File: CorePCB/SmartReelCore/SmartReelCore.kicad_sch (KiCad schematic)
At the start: 5 parts, among them J1 Screw_Terminal_01x02, J2 Screw_Terminal_01x03, J3 Screw_Terminal_01x04

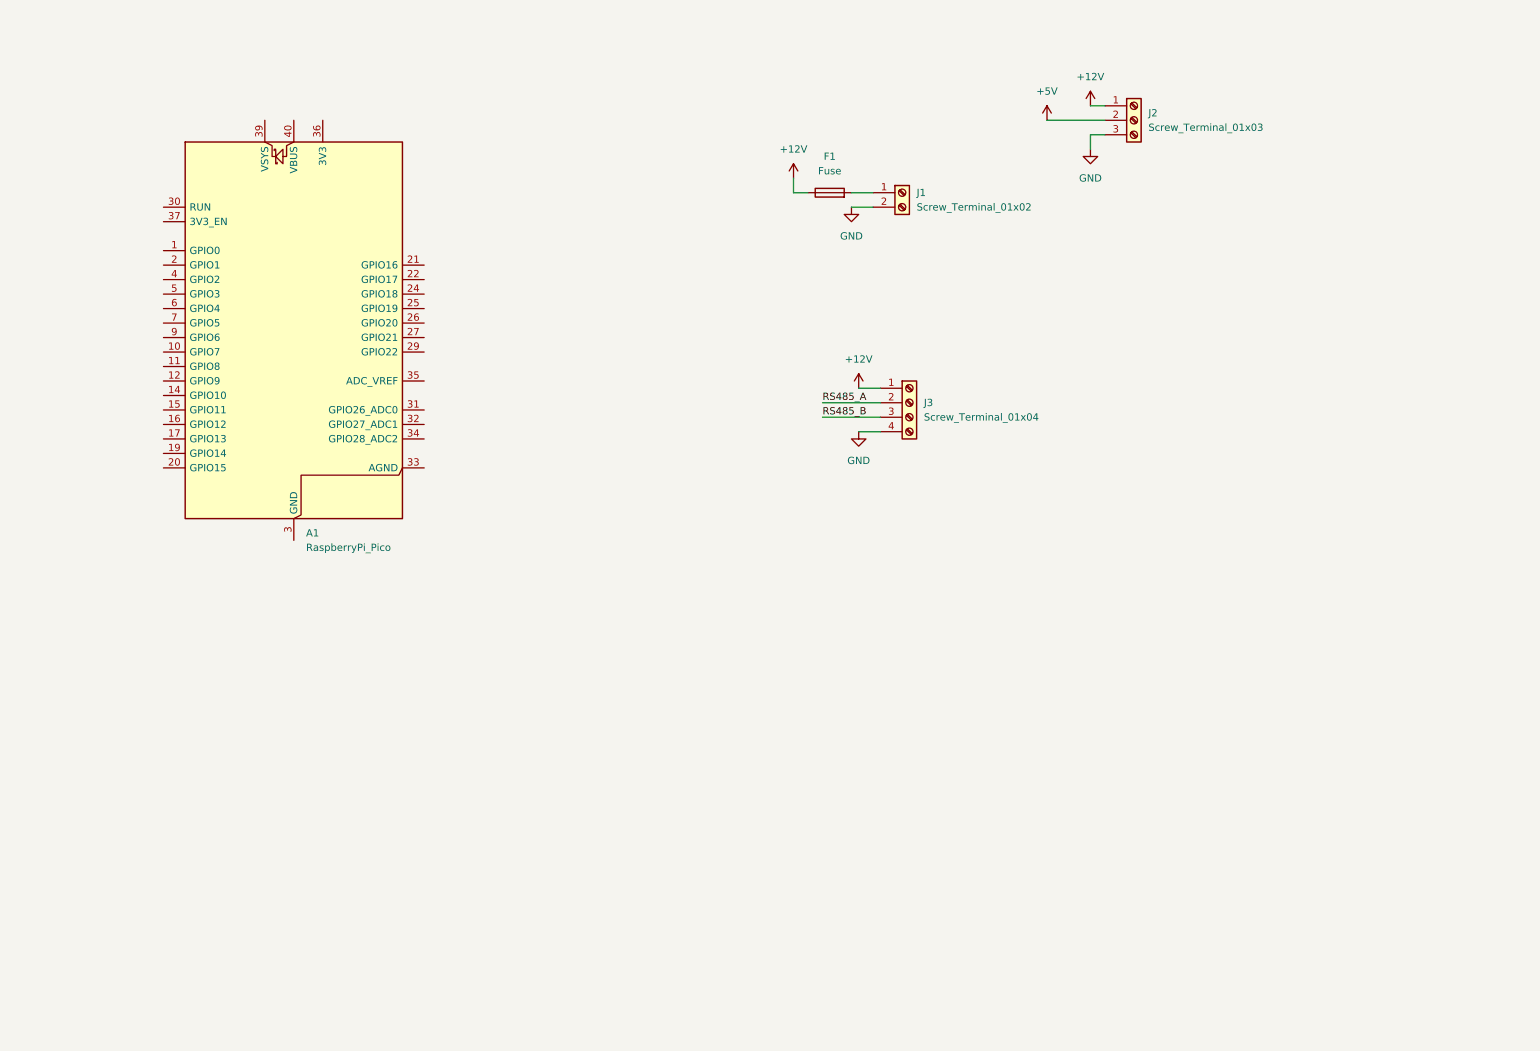
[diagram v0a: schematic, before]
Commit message: Rev 1 PCBs ordered
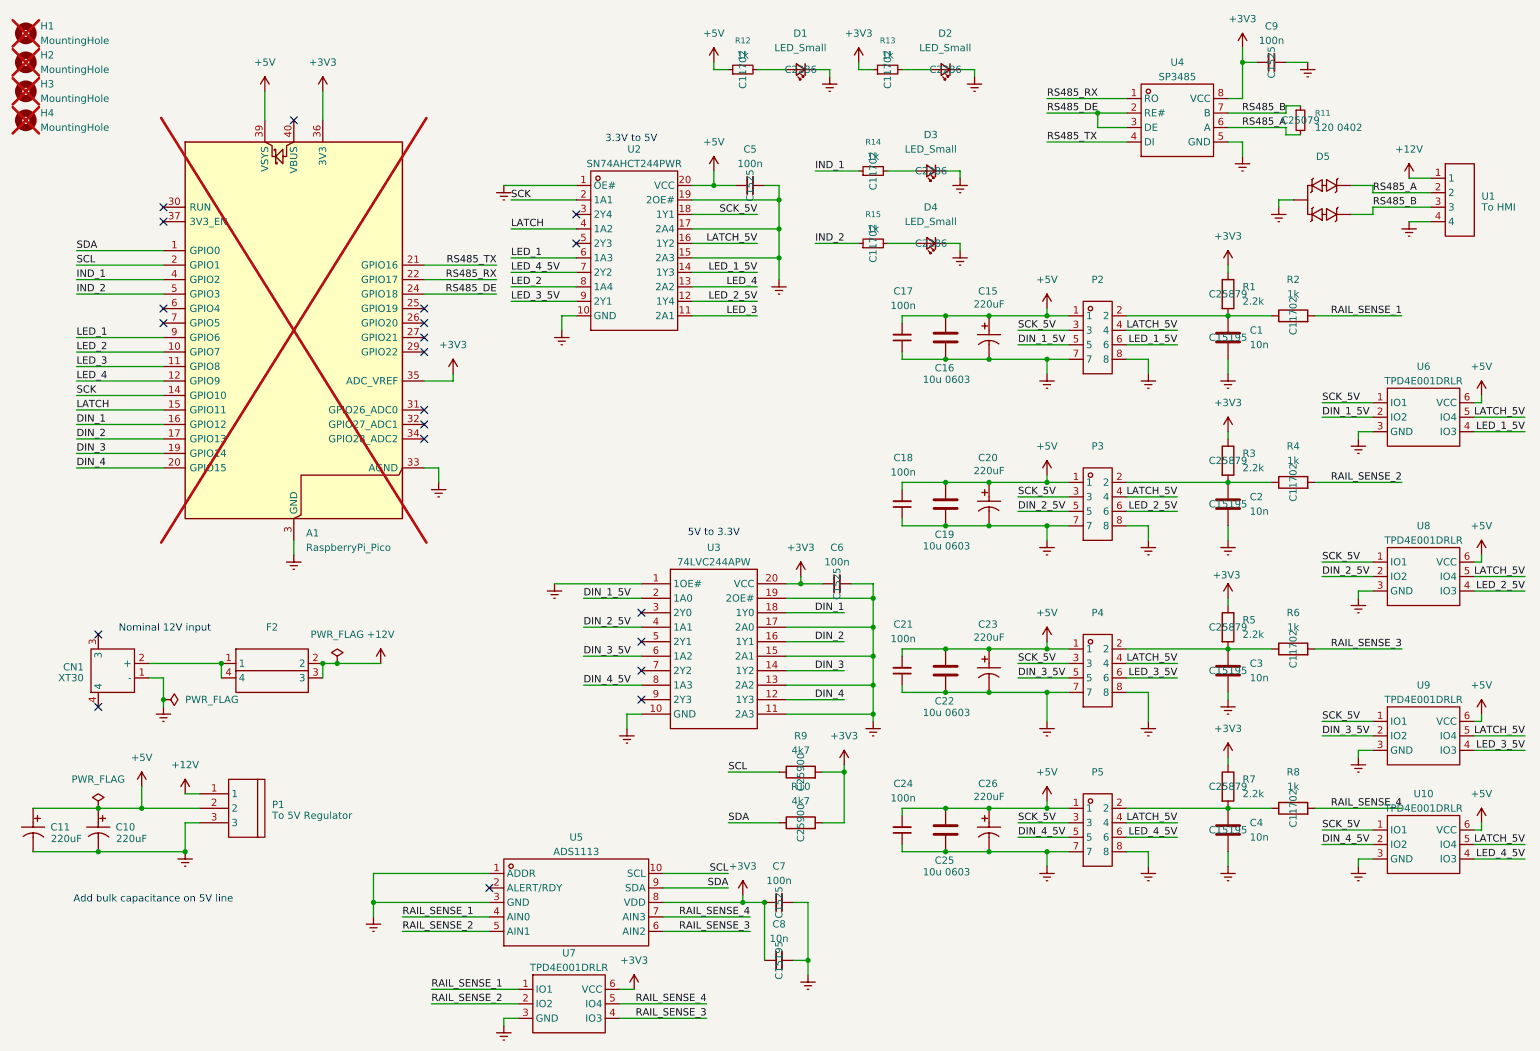
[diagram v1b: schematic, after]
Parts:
- removed F1: Fuse, symbol Device:Fuse
- removed J1: Screw_Terminal_01x02, symbol Connector:Screw_Terminal_01x02
- removed J2: Screw_Terminal_01x03, symbol Connector:Screw_Terminal_01x03
- removed J3: Screw_Terminal_01x04, symbol Connector:Screw_Terminal_01x04
- added C1, C2, C3, C4: 10n, Capacitor_SMD:C_0402_1005Metric, symbol Device:C
- added C10, C11, C15, C20, C23, C26: 220uF, EasyEDA_Lib:CAP-SMD_BD8.0-L8.3-W8.3-LS9.3-FD, symbol EasyEDA_Lib:RVT1V221M0810-C72498
- added C16, C19, C22, C25: 10u 0603, Capacitor_SMD:C_0603_1608Metric, symbol Device:C
- added C17, C18, C21, C24, C5, C6, C7, C9: 100n, Capacitor_SMD:C_0402_1005Metric, symbol Device:C_Small
- added C8: 10n, Capacitor_SMD:C_0402_1005Metric, symbol Device:C_Small
- added CN1: XT30, EasyEDA_Lib:CONN-TH_XT30PW-M, symbol EasyEDA_Lib:XT30PW-M
- added D1, D2, D3, D4: LED_Small, LED_SMD:LED_0603_1608Metric, symbol Device:LED_Small
- added D5: ~, EasyEDA_Lib:SOT-23-3_L2.9-W1.3-P1.90-LS2.4-BR, symbol EasyEDA_Lib:SM712-02HTG_C3008057
- added F2: ~, EasyEDA_Lib:FUSE-TH_4P-L16.0-W6.7, symbol EasyEDA_Lib:XF-508P-B-B
- added H1, H2, H3, H4: MountingHole, MountingHole:MountingHole_3.2mm_M3_Pad, symbol Mechanical:MountingHole
- added P1: To 5V Regulator, EasyEDA_Lib:CONN-TH_3P-P5.00_WJ500V-5.08-3P, symbol EasyEDA_Lib:WJ500V-5.08-3P-14-00A
- added P2, P3, P4, P5: ~, EasyEDA_Lib:IDC-TH_8P-P2.00_BOOMELE2X4P, symbol EasyEDA_Lib:IDC Box 2X4P
- added R1, R3, R5, R7: 2.2k, Resistor_SMD:R_0402_1005Metric, symbol Device:R
- added R10, R9: 4k7, Resistor_SMD:R_0402_1005Metric, symbol Device:R
- added R11: 120 0402, Resistor_SMD:R_0402_1005Metric, symbol Device:R_Small
- added R12, R13, R14, R15: 1k, Resistor_SMD:R_0402_1005Metric, symbol Device:R_Small
- added R2, R4, R6, R8: 1k, Resistor_SMD:R_0402_1005Metric, symbol Device:R
- added U1: To HMI, EasyEDA_Lib:CONN-TH_WJ500V-5.08-4P, symbol EasyEDA_Lib:WJ500V-5.08-4P
- added U10, U6, U7, U8, U9: TPD4E001DRLR, EasyEDA_Lib:SOT-563_L1.6-W1.2-P0.50-LS1.6-BL, symbol EasyEDA_Lib:TPD4E001DRLR_C2987155
- added U2: SN74AHCT244PWR, EasyEDA_Lib:TSSOP-20_L6.5-W4.4-P0.65-LS6.4-BL, symbol EasyEDA_Lib:SN74AHCT244PWR
- added U3: 74LVC244APW, EasyEDA_Lib:TSSOP-20_L6.5-W4.4-P0.65-LS6.4-BL, symbol EasyEDA_Lib:74LVC244APW,118
- added U4: SP3485, EasyEDA_Lib:SOIC-8_L5.0-W4.0-P1.27-LS6.0-BL, symbol EasyEDA_Lib:SP3485EN-L/TR
- added U5: ADS1113, EasyEDA_Lib:VSSOP-10_L3.0-W3.0-P0.50-LS4.9-BL, symbol EasyEDA_Lib:ADS1115IDGST
- A1: now not fitted
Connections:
- net +12V: now also F2.2, F2.3, P1.1, U1.1
- net +5V: now also A1.39 (VSYS), C10.1, C11.1, C15.1, C16.1, C17.2, C18.2, C19.1, C20.1, C21.2, C22.1, C23.1, C24.2, C25.1, C26.1, C5.1, P1.2, P2.1, P3.1, P4.1, P5.1, R12.1, U10.6 (VCC), U2.20 (VCC), U6.6 (VCC), U8.6 (VCC), U9.6 (VCC)
- net RS485_A: now also D5.1, R11.2, U1.2, U4.6 (A)
- net RS485_B: now also D5.2, R11.1, U1.3, U4.7 (B)
- net SDA: now reaches A1.1 (GPIO0)
- net SDA: now also R10.1, U5.9 (SDA)
- net LED_2: now reaches A1.10 (GPIO7)
- net LED_2: now also U2.8 (1A4)
- net LED_3: now reaches A1.11 (GPIO8)
- net LED_3: now also U2.11 (2A1)
- net LED_4: now reaches A1.12 (GPIO9)
- net LED_4: now also U2.13 (2A2)
- net Earth: now reaches A1.13 (GND), A1.18 (GND), A1.23 (GND), A1.28 (GND), A1.3 (GND), A1.38 (GND), A1.8 (GND)
- net Earth: now also A1.33 (AGND), C1.2, C10.2, C11.2, C15.2, C16.2, C17.1, C18.1, C19.2, C2.2, C20.2, C21.1, C22.2, C23.2, C24.1, C25.2, C26.2, C3.2, C4.2, C5.2, C6.2, C7.2, C8.2, C9.2, CN1.1 (-), D1.1 (K), D2.1 (K), D3.1 (K), D4.1 (K), D5.3, P1.3, P2.7, P2.8, P3.7, P3.8, P4.7, P4.8, P5.7, P5.8, U1.4, U10.3 (GND), U2.1 (OE#), U2.10 (GND), U2.15 (2A3), U2.17 (2A4), U2.19 (2OE#), U3.1 (1OE#), U3.10 (GND), U3.11 (2A3), U3.13 (2A2), U3.15 (2A1), U3.17 (2A0), U3.19 (2OE#), U4.5 (GND), U5.1 (ADDR), U5.3 (GND), U6.3 (GND), U7.3 (GND), U8.3 (GND), U9.3 (GND)
- net SCK: now reaches A1.14 (GPIO10)
- net SCK: now also U2.2 (1A1)
- net LATCH: now reaches A1.15 (GPIO11)
- net LATCH: now also U2.4 (1A2)
- net DIN_1: now reaches A1.16 (GPIO12)
- net DIN_1: now also U3.18 (1Y0)
- net DIN_2: now reaches A1.17 (GPIO13)
- net DIN_2: now also U3.16 (1Y1)
- net DIN_3: now reaches A1.19 (GPIO14)
- net DIN_3: now also U3.14 (1Y2)
- net SCL: now reaches A1.2 (GPIO1)
- net SCL: now also R9.1, U5.10 (SCL)
- net DIN_4: now reaches A1.20 (GPIO15)
- net DIN_4: now also U3.12 (1Y3)
- net RS485_TX: now reaches A1.21 (GPIO16)
- net RS485_TX: now also U4.4 (DI)
- net RS485_RX: now reaches A1.22 (GPIO17)
- net RS485_RX: now also U4.1 (RO)
- net RS485_DE: now reaches A1.24 (GPIO18)
- net RS485_DE: now also U4.2 (RE#), U4.3 (DE)
- net +3V3: now reaches A1.35 (ADC_VREF)
- net +3V3: now also A1.36 (3V3), C6.1, C7.1, C8.1, C9.1, R1.1, R10.2, R13.1, R3.1, R5.1, R7.1, R9.2, U3.20 (VCC), U4.8 (VCC), U5.8 (VDD), U7.6 (VCC)
- net IND_1: now reaches A1.4 (GPIO2)
- net IND_1: now also R14.1
- net IND_2: now reaches A1.5 (GPIO3)
- net IND_2: now also R15.1
- net LED_1: now reaches A1.9 (GPIO6)
- net LED_1: now also U2.6 (1A3)
- new net: C1.1, P2.2, R1.2, R2.1
- new net: C2.1, P3.2, R3.2, R4.1
- new net: D1.2 (A), R12.2
- new net: C3.1, P4.2, R5.2, R6.1
- new net: D3.2 (A), R14.2
- new net: CN1.2 (+), F2.1, F2.4
- new net: C4.1, P5.2, R7.2, R8.1
- new net: D4.2 (A), R15.2
- new net: D2.2 (A), R13.2
- new net DIN_1_5V: P2.5, U3.2 (1A0), U6.2 (IO2)
- new net DIN_2_5V: P3.5, U3.4 (1A1), U8.2 (IO2)
- new net DIN_3_5V: P4.5, U3.6 (1A2), U9.2 (IO2)
- new net DIN_4_5V: P5.5, U10.2 (IO2), U3.8 (1A3)
- new net LATCH_5V: P2.4, P3.4, P4.4, P5.4, U10.5 (IO4), U2.16 (1Y2), U6.5 (IO4), U8.5 (IO4), U9.5 (IO4)
- new net LED_1_5V: P2.6, U2.14 (1Y3), U6.4 (IO3)
- new net LED_2_5V: P3.6, U2.12 (1Y4), U8.4 (IO3)
- new net LED_3_5V: P4.6, U2.9 (2Y1), U9.4 (IO3)
- new net LED_4_5V: P5.6, U10.4 (IO3), U2.7 (2Y2)
- new net RAIL_SENSE_1: R2.2, U5.4 (AIN0), U7.1 (IO1)
- new net RAIL_SENSE_2: R4.2, U5.5 (AIN1), U7.2 (IO2)
- new net RAIL_SENSE_3: R6.2, U5.6 (AIN2), U7.4 (IO3)
- new net RAIL_SENSE_4: R8.2, U5.7 (AIN3), U7.5 (IO4)
- new net SCK_5V: P2.3, P3.3, P4.3, P5.3, U10.1 (IO1), U2.18 (1Y1), U6.1 (IO1), U8.1 (IO1), U9.1 (IO1)
- no-connect marks 0 -> 21
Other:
- note added: "3.3V to 5V"
- note added: "5V to 3.3V"
- note added: "Add bulk capacitance on 5V line"
- note added: "Nominal 12V input"
